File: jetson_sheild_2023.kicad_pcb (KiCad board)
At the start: 2 copper layers, 72 x 47.5 mm, 19 parts, among them IC1 TJA1441AT_0Z, J1 JetsonOrinNano_DevKit_J12, J10 BlockDetectLimSw_Rear, J2 VL53L1X_front, J3 VL53L1X_middle, J4 VL53L1X_rear, J5 BlockDetectLimSw_Front, J6 BlockDetectLimSw_MiddleOn, J7 BlockDetectLimSw_MiddleOff, J8 Conn_01x04_Socket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

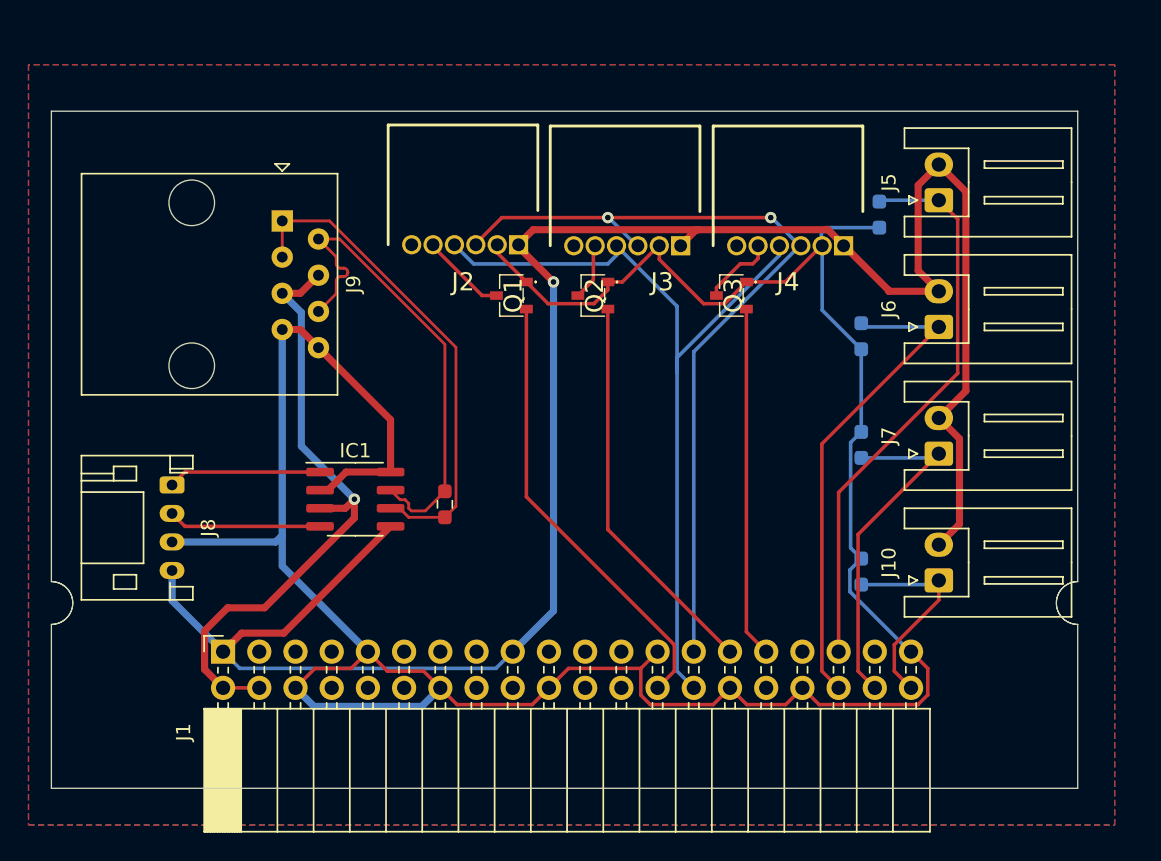
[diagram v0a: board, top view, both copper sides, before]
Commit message: ZHコネクタをPHコネクタに変更,電源ボタンと汎用ボタンを追加,バージョンとロゴを印字
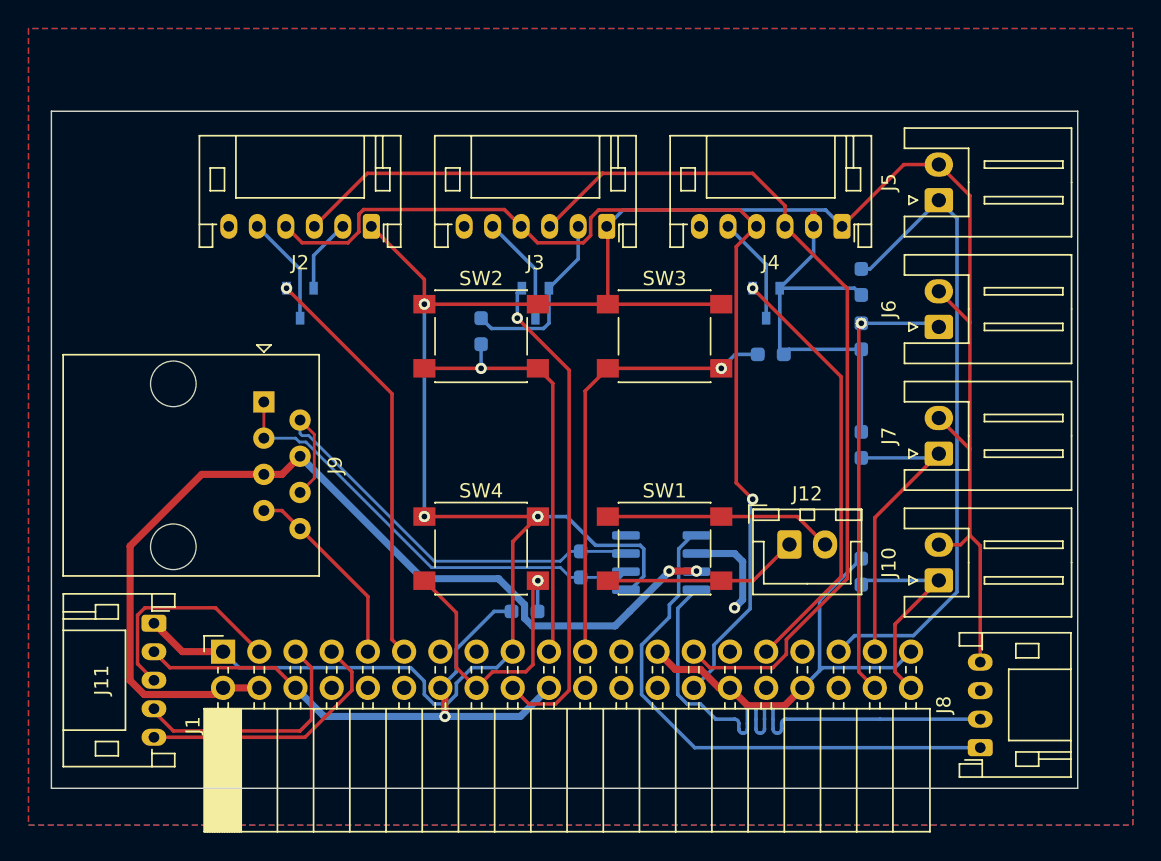
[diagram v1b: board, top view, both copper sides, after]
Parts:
- added G***: LOGO, d_robo_lib:robocon, B.Cu at (104.1, 102.4)
- added J11: BNO055, Connector_JST:JST_PH_S5B-PH-K_1x05_P2.00mm_Horizontal, F.Cu at (107.9, 112.8)
- added J12: PWR, Connector_JST:JST_XH_B2B-XH-A_1x02_P2.50mm_Vertical, F.Cu at (152.4, 107.3)
- added R6: 1K, Resistor_SMD:R_0603_1608Metric_Pad0.98x0.95mm_HandSolder, B.Cu at (130.8, 92.4)
- added R7: 1K, Resistor_SMD:R_0603_1608Metric_Pad0.98x0.95mm_HandSolder, B.Cu at (151.1, 94.0)
- added R8: 1K, Resistor_SMD:R_0603_1608Metric_Pad0.98x0.95mm_HandSolder, B.Cu at (133.9, 112.0)
- added SW1: PWR_BTN, Button_Switch_SMD:SW_SPST_PTS645, F.Cu at (143.7, 107.6)
- added SW2: PERI_BTN1, Button_Switch_SMD:SW_SPST_PTS645, F.Cu at (130.8, 92.7)
- added SW3: PERI_BTN2, Button_Switch_SMD:SW_SPST_PTS645, F.Cu at (143.7, 92.7)
- added SW4: PERI_BTN3, Button_Switch_SMD:SW_SPST_PTS645, F.Cu at (130.8, 107.6)
- IC1, Q1, Q2, Q3, R4: moved to B.Cu
- J2, J3, J4: footprint samacsys_lib:SHDRRA6W50P0X150_1X6_1050X600X370P -> Connector_JST:JST_PH_S6B-PH-K_1x06_P2.00mm_Horizontal
- moved J8 59.6 mm to (165.8, 121.6), turned to 90 degrees
- moved IC1 21.9 mm to (143.4, 108.6), turned to 180 degrees
- moved Q1 14.8 mm to (118.1, 90.4), turned to 0 degrees
- moved J9 12.8 mm to (115.6, 97.3)
- moved R4 10.4 mm to (137.8, 108.7)
- moved J4 7.66 mm to (156.1, 85.0), turned to 180 degrees
- moved R1 4.89 mm to (157.5, 88.9)
- moved Q2 4.07 mm to (134.6, 90.4), turned to 0 degrees
- moved J2 2.97 mm to (123.1, 85.0), turned to 180 degrees
- moved J3 2.81 mm to (139.6, 85.0), turned to 180 degrees
- moved Q3 2.50 mm to (150.8, 90.4), turned to 0 degrees
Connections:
- J1 pad 11: unconnected-(J1-RTS1/GPIO(112)-Pad11) -> XSHUT0
- J1 pad 16: unconnected-(J1-1_CS1/GPIO(126)-Pad16) -> PERIPHERAL_BTN3
- J1 pad 18: unconnected-(J1-1_CS0/GPIO(125)-Pad18) -> XSHUT1
- J1 pad 19: unconnected-(J1-MOSI0/GPIO(135)-Pad19) -> PERIPHERAL_BTN1
- J1 pad 21: unconnected-(J1-MISO0/GPIO(134)-Pad21) -> PERIPHERAL_BTN2
- J1 pad 26: XSHUT0 -> unconnected-(J1-0_CS1/GPIO(137)-Pad26)
- J1 pad 29: XSHUT1 -> unconnected-(J1-GPIO01(105)-Pad29)
- J1 pad 3: unconnected-(J1-SDA1-Pad3) -> SDA1
- J1 pad 36: BlockDetect_MiddleOn -> unconnected-(J1-CTS1/GPIO(113)-Pad36)
- J1 pad 37: unconnected-(J1-MOSI1/GPIO(124)-Pad37) -> BlockDetect_MiddleOff
- J1 pad 38: BlockDetect_MiddleOff -> BlockDetect_MiddleOn
- J1 pad 5: unconnected-(J1-SCL1-Pad5) -> SCL1
- J1 pad 7: unconnected-(J1-MCLK/GPIO9(144)-Pad7) -> BNO055_RESET
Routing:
- net GND: track 189.4 -> 137.6 mm, vias 0 -> 2
- net PERIPHERAL_BTN2: track 0.00 -> 31.5 mm, vias 0 -> 1
- net +3V3: track 147.9 -> 179.1 mm, vias 1 -> 3
- net PERIPHERAL_BTN1: track 0.00 -> 30.3 mm, vias 0 -> 1
- net CANTX: track 10.8 -> 38.2 mm
- net CANRX: track 10.8 -> 38.0 mm
- net SDA0: track 58.8 -> 83.2 mm, vias 2 -> 0
- net +5V: track 44.5 -> 68.6 mm, vias 1 -> 2
- net PERIPHERAL_BTN3: track 0.00 -> 21.9 mm, vias 0 -> 1
- net BNO055_RESET: track 0.00 -> 18.5 mm
- net SCL1: track 0.00 -> 17.4 mm
- net Net-(J12-Pin_2): track 0.00 -> 16.1 mm
- net SCL0: track 58.0 -> 73.4 mm, vias 0 -> 1
- net SDA1: track 0.00 -> 15.1 mm
- net Net-(J12-Pin_1): track 0.00 -> 13.8 mm
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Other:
- outline, holes or cut-outs redrawn
- board text added: "2023 nityc-d-robo Jetson Sheild ver1.1"
